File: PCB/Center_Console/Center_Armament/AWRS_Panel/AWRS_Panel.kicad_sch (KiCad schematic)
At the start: 0 parts

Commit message: Add AWRS_Panel schematic; refresh symbol caches
AWRS_Panel: 2-sheet hierarchical breakout board schematic.
Root sheet: ADS1115 @ 0x48 (ADDR→GND), three RC-filtered analog inputs
(A0=QTY, A1=DROP INTVL, A2=MODE SEL), 1kΩ+100nF per input, three 4-pin
JST-XH pot connectors (J1/J3/J5), 6-pin JST-XH MCU harness (J2), VDD
decoupling (C1 100nF + C2 10µF), status LED (D1+R22), PWR_FLAGs.
Backlighting sheet: 3 LED strings × 5 LEDs, 3×120Ω resistors, 2-pin
Mini-Fit Jr (J_LED). Controls sheet: placeholder — panel-mounted switch
types and position counts deferred until extracted from DCS sim.

MCU_CAN.kicad_sch, Misc_Switch_Panel.kicad_sch: symbol cache refresh
from IRLML2502 library rework.
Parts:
- added C1: 100nF, symbol Device:C
- added C2: 10uF, symbol Device:C
- added D1: POWER_ST, LED_SMD:LED_0805_2012Metric, symbol Device:LED
- added J1: QTY POT, symbol Connector_Generic:Conn_01x04
- added J2: MAIN_ARMAMENT_PANEL, symbol Connector_Generic:Conn_01x06
- added J3: DROP INTVL, symbol Connector_Generic:Conn_01x04
- added J5: MODE SEL, symbol Connector_Generic:Conn_01x04
- added R22: 3.3k, Resistor_SMD:R_0805_2012Metric, symbol Device:R
- added U1: ADS1115IDGS, Package_SO:TSSOP-10_3x3mm_P0.5mm, symbol Analog_ADC:ADS1115IDGS
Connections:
- new net: D1.2 (A), R22.2
- new net +3.3V: C1.1, C2.1, J1.1 (Pin_1), J2.5 (Pin_5), J3.1 (Pin_1), J5.1 (Pin_1), R22.1, U1.8 (VDD)
- new net DROP INTVL WIPER: J3.2 (Pin_2), U1.5 (AIN1)
- new net GND: C1.2, C2.2, D1.1 (K), J1.3 (Pin_3), J1.4 (Pin_4), J2.3 (Pin_3), J2.4 (Pin_4), J3.3 (Pin_3), J3.4 (Pin_4), J5.3 (Pin_3), J5.4 (Pin_4), U1.1 (ADDR), U1.3 (GND)
- new net MODE SEL WIPER: J5.2 (Pin_2), U1.6 (AIN2)
- new net QTY POT WIPER: J1.2 (Pin_2), U1.4 (AIN0)
- new net SCL: J2.2 (Pin_2), U1.10 (SCL)
- new net SDA: J2.1 (Pin_1), U1.9 (SDA)
- no-connect marks 0 -> 3
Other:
- added sheet Backlighting (Backlighting.kicad_sch)
- added sheet Controls (Controls.kicad_sch)
- note added: "Status LED Indicators"

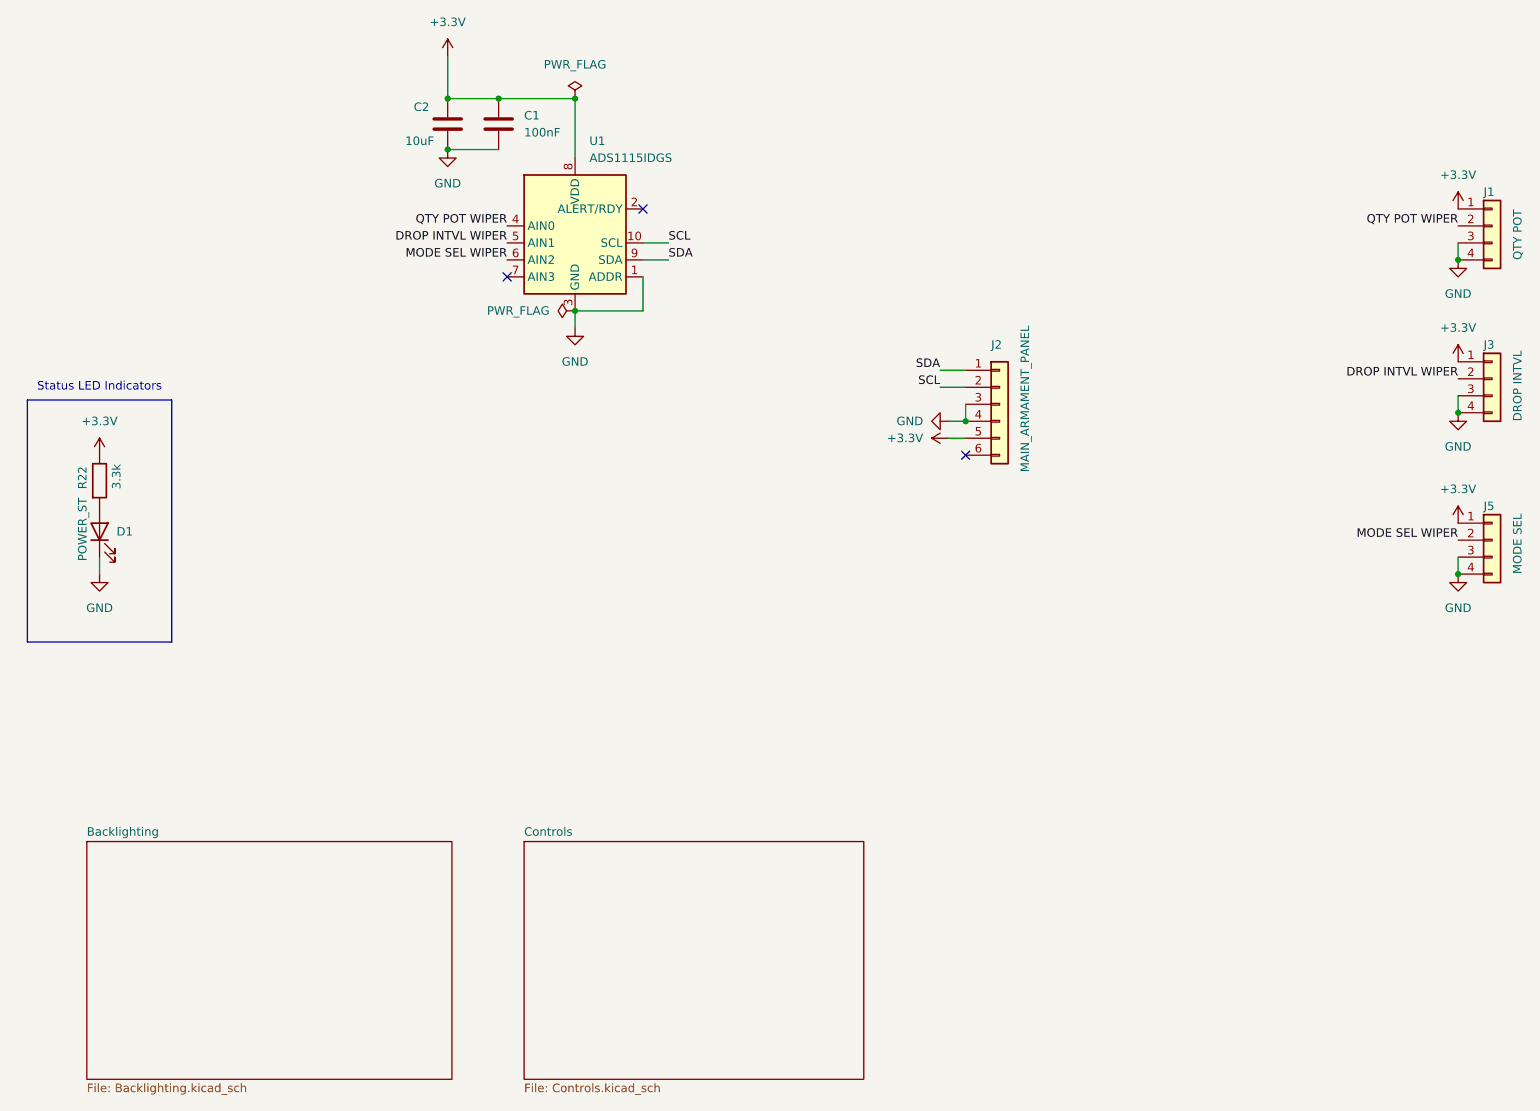
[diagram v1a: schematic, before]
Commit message: chore: ignore .claire/ and .vscode/ dirs; save AWRS_Panel schematic state
- Expand .gitignore: add .claire/ (Claude Code worktrees), consolidate
  scattered .vscode/ file rules into a single **/.vscode/ glob
- AWRS_Panel.kicad_sch / Controls.kicad_sch: KiCad expanded embedded
  lib_symbols on open/save (Device:C_Small etc.)
- AWRS_Panel.kicad_pro: used_designators reset by KiCad on save
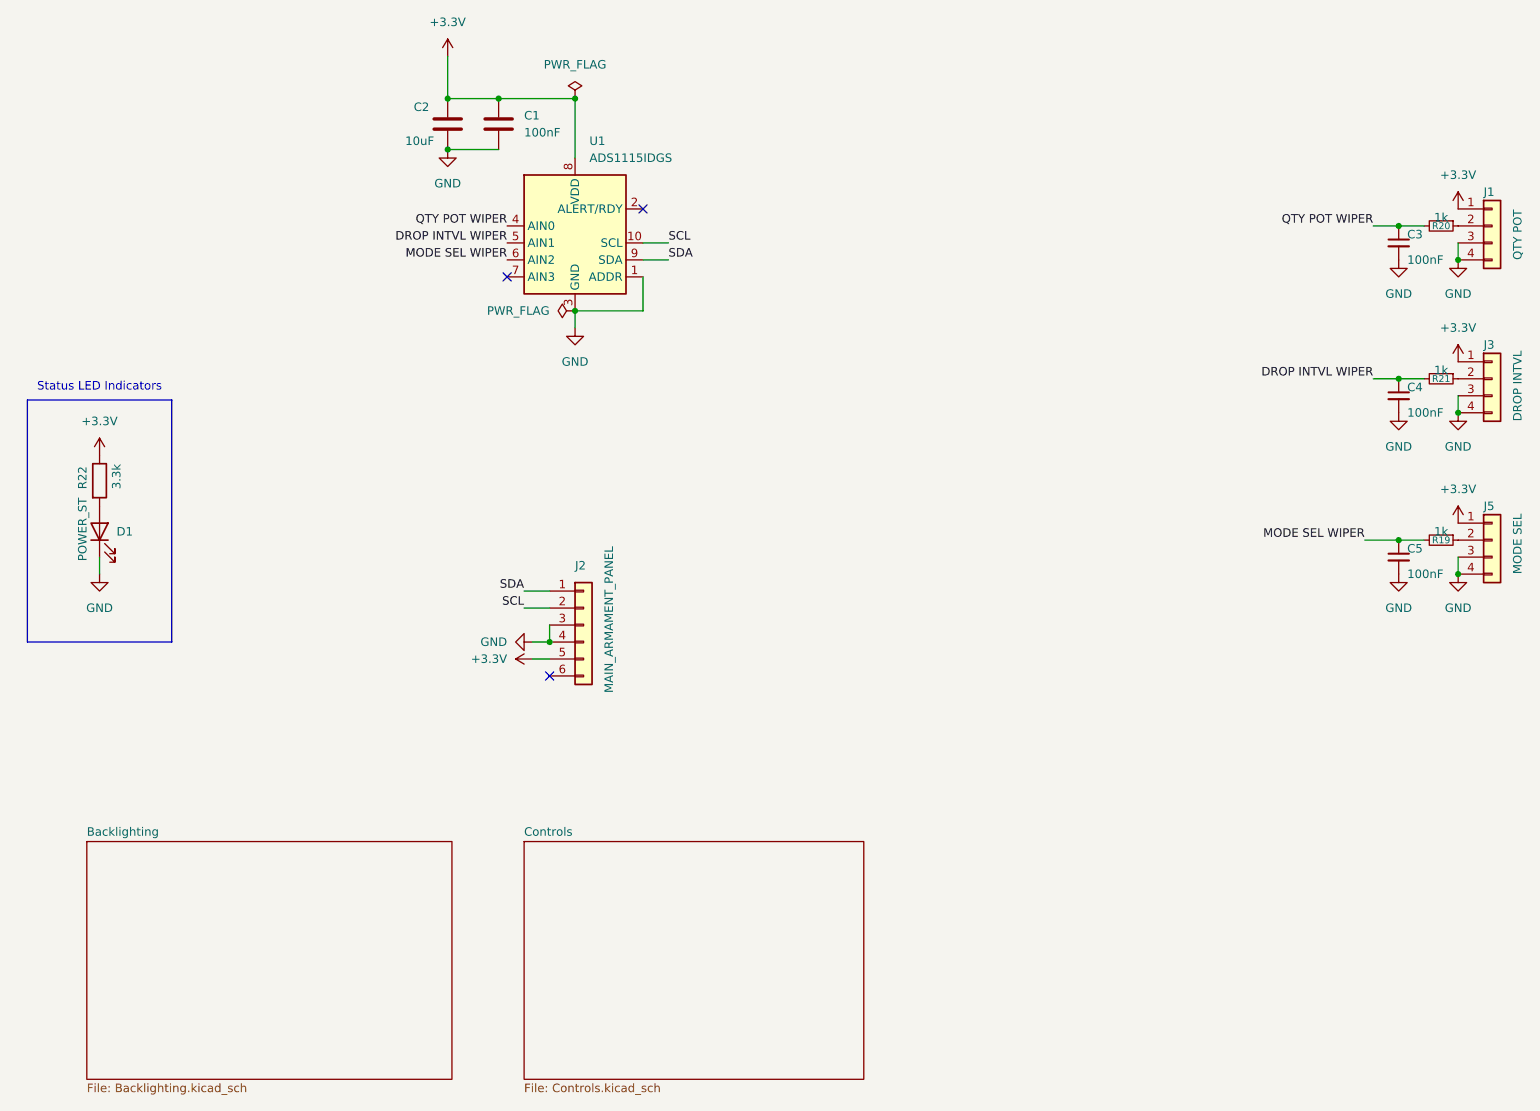
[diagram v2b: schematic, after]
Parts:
- added C3, C4, C5: 100nF, symbol Device:C_Small
- added R19, R20, R21: 1k, symbol Device:R_Small
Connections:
- net DROP INTVL WIPER: now also C4.1, R21.2; no longer J3.2 (Pin_2)
- net GND: now also C3.2, C4.2, C5.2
- net MODE SEL WIPER: now also C5.1, R19.2; no longer J5.2 (Pin_2)
- net QTY POT WIPER: now also C3.1, R20.2; no longer J1.2 (Pin_2)
- new net: J3.2 (Pin_2), R21.1
- new net: J1.2 (Pin_2), R20.1
- new net: J5.2 (Pin_2), R19.1
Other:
- moved on the sheet: J2
